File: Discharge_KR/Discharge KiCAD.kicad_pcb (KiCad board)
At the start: 2 copper layers, 64.3 x 47.9 mm, 20 parts, among them J1 Conn_01x02, J2 Conn_01x02, J3 Conn_01x02, J4 Conn_01x03, K1 DBR71210, U1 MCP1703AT-3302E/MBVAO, U2 HCPL-817-000E

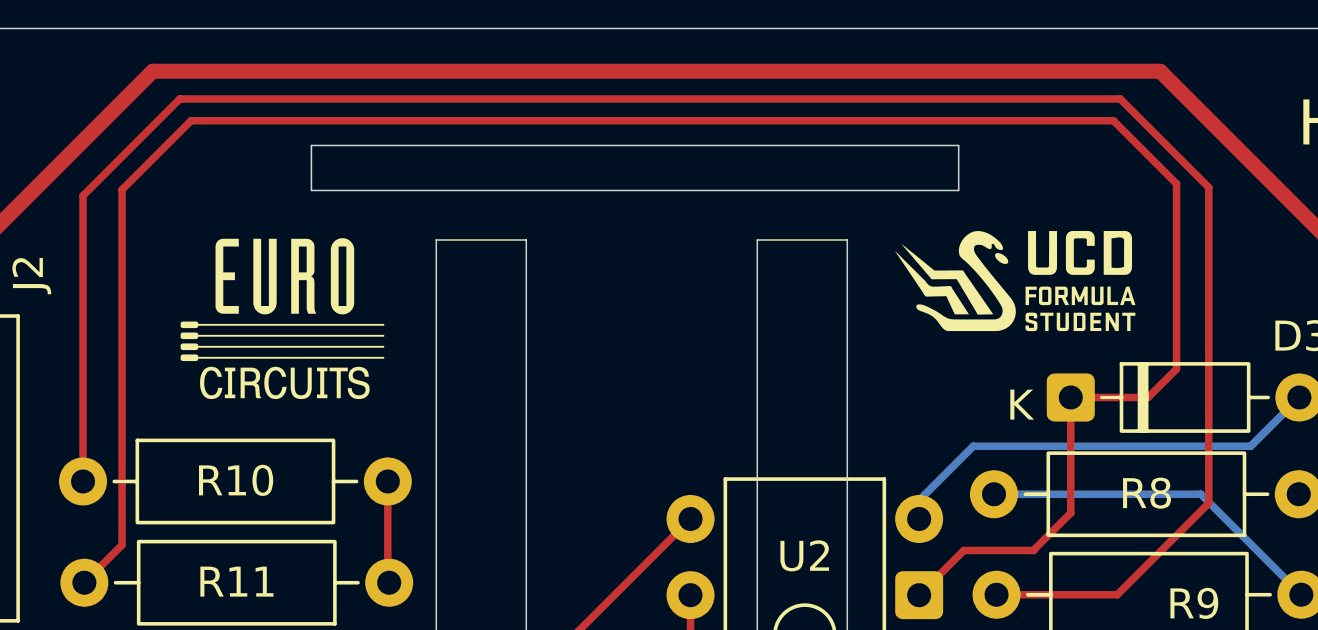
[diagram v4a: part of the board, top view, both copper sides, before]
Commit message: Slave with SMD and no other fuses
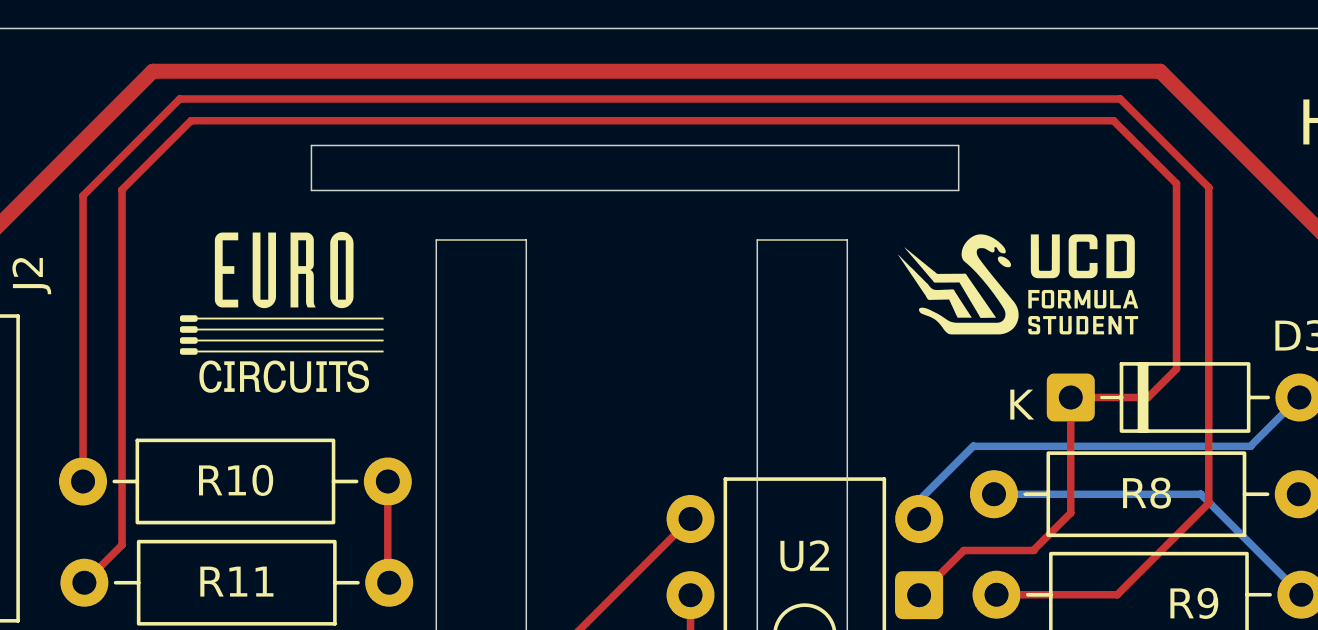
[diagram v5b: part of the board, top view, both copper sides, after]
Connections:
- net Discharging_N renamed Discharing_N
- net TS+ renamed Load+
- net TS- renamed Load-
